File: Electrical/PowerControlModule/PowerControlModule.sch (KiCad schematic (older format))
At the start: 1 part, among them Q1 IPP120P04P4L03AKSA1

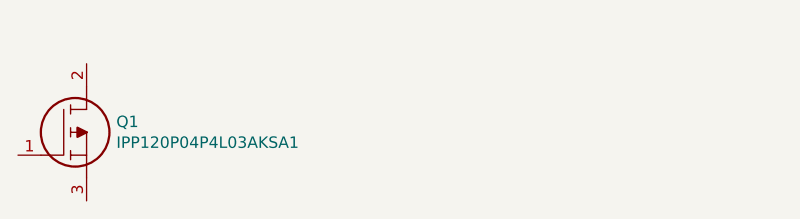
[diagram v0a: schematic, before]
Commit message: Testing import of power mosfet
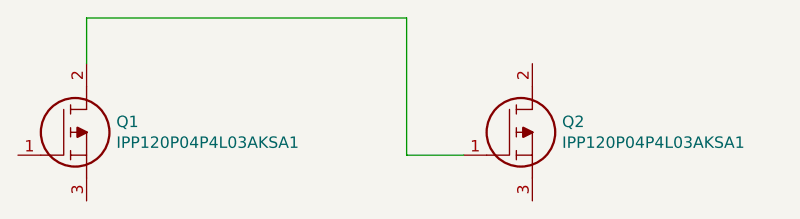
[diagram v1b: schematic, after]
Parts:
- added Q2: IPP120P04P4L03AKSA1, TO254P440X1000X2110-3P, symbol LibraryLoader:IPP120P04P4L03AKSA1
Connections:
- net at Q1.2: now also Q2.1
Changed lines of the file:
@@
 	1    0    0    -1
 $EndComp
+$Comp
+L LibraryLoader:IPP120P04P4L03AKSA1 Q2
+U 1 1 5D7A9CCC
+P 7700 3350
+F 0 "Q2" H 8130 3496 50  0000 L CNN
+F 1 "IPP120P04P4L03AKSA1" H 8130 3405 50  0000 L CNN
+F 2 "TO254P440X1000X2110-3P" H 8150 3300 50  0001 L CNN
+F 3 "https://componentsearchengine.com/Datasheets/1/IPP120P04P4L03AKSA1.pdf" H 8150 3200 50  0001 L CNN
+F 4 "MOSFET P-Ch 40V 120A OptiMOS-P2 TO-220" H 8150 3100 50  0001 L CNN "Description"
+F 5 "4.4" H 8150 3000 50  0001 L CNN "Height"
+F 6 "726-IPP120P04P4L03AK" H 8150 2900 50  0001 L CNN "Mouser Part Number"
+F 7 "https://www.mouser.com/Search/Refine.aspx?Keyword=726-IPP120P04P4L03AK" H 8150 2800 50  0001 L CNN "Mouser Price/Stock"
+F 8 "Infineon" H 8150 2700 50  0001 L CNN "Manufacturer_Name"
+F 9 "IPP120P04P4L03AKSA1" H 8150 2600 50  0001 L CNN "Manufacturer_Part_Number"
+	1    7700 3350
+	1    0    0    -1
+$EndComp
+Wire Wire Line
+	7700 3350 7450 3350
+Wire Wire Line
+	7450 3350 7450 2750
+Wire Wire Line
+	7450 2750 6050 2750
+Wire Wire Line
+	6050 2750 6050 2950
 $EndSCHEMATC

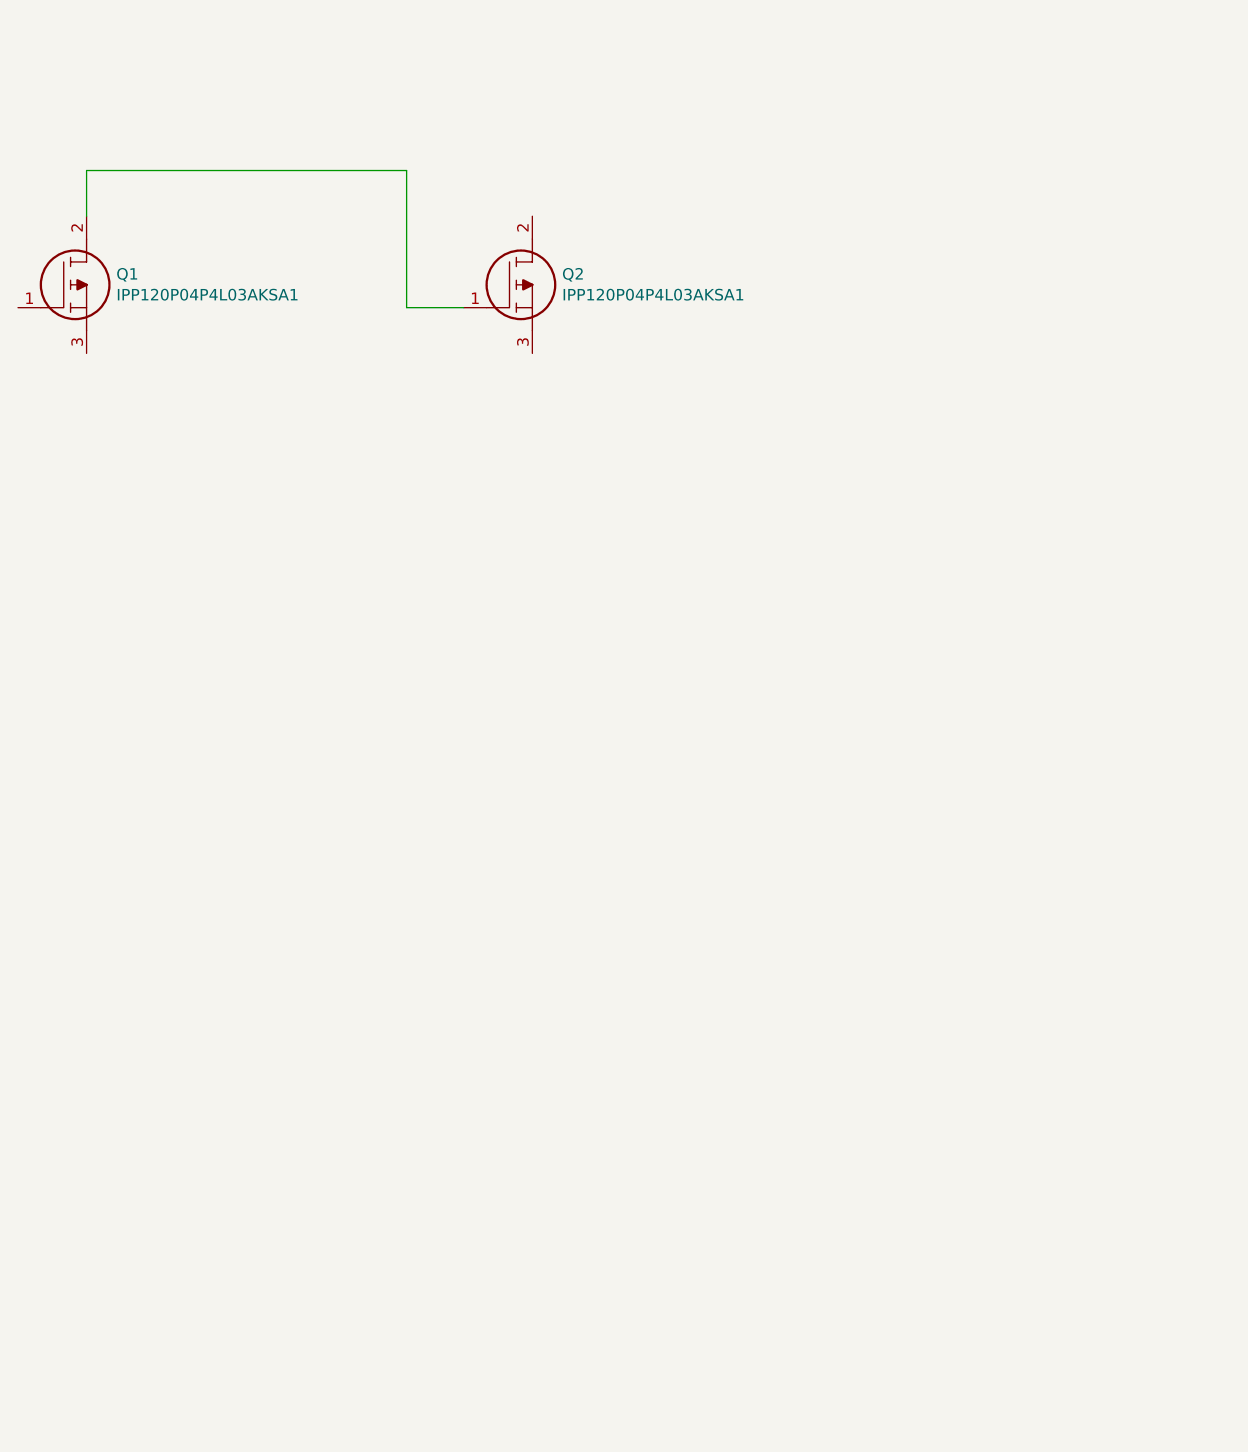
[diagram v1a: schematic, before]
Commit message: Lays out peripherals and motor control power distribution
Paginates the schematic for ease of editing
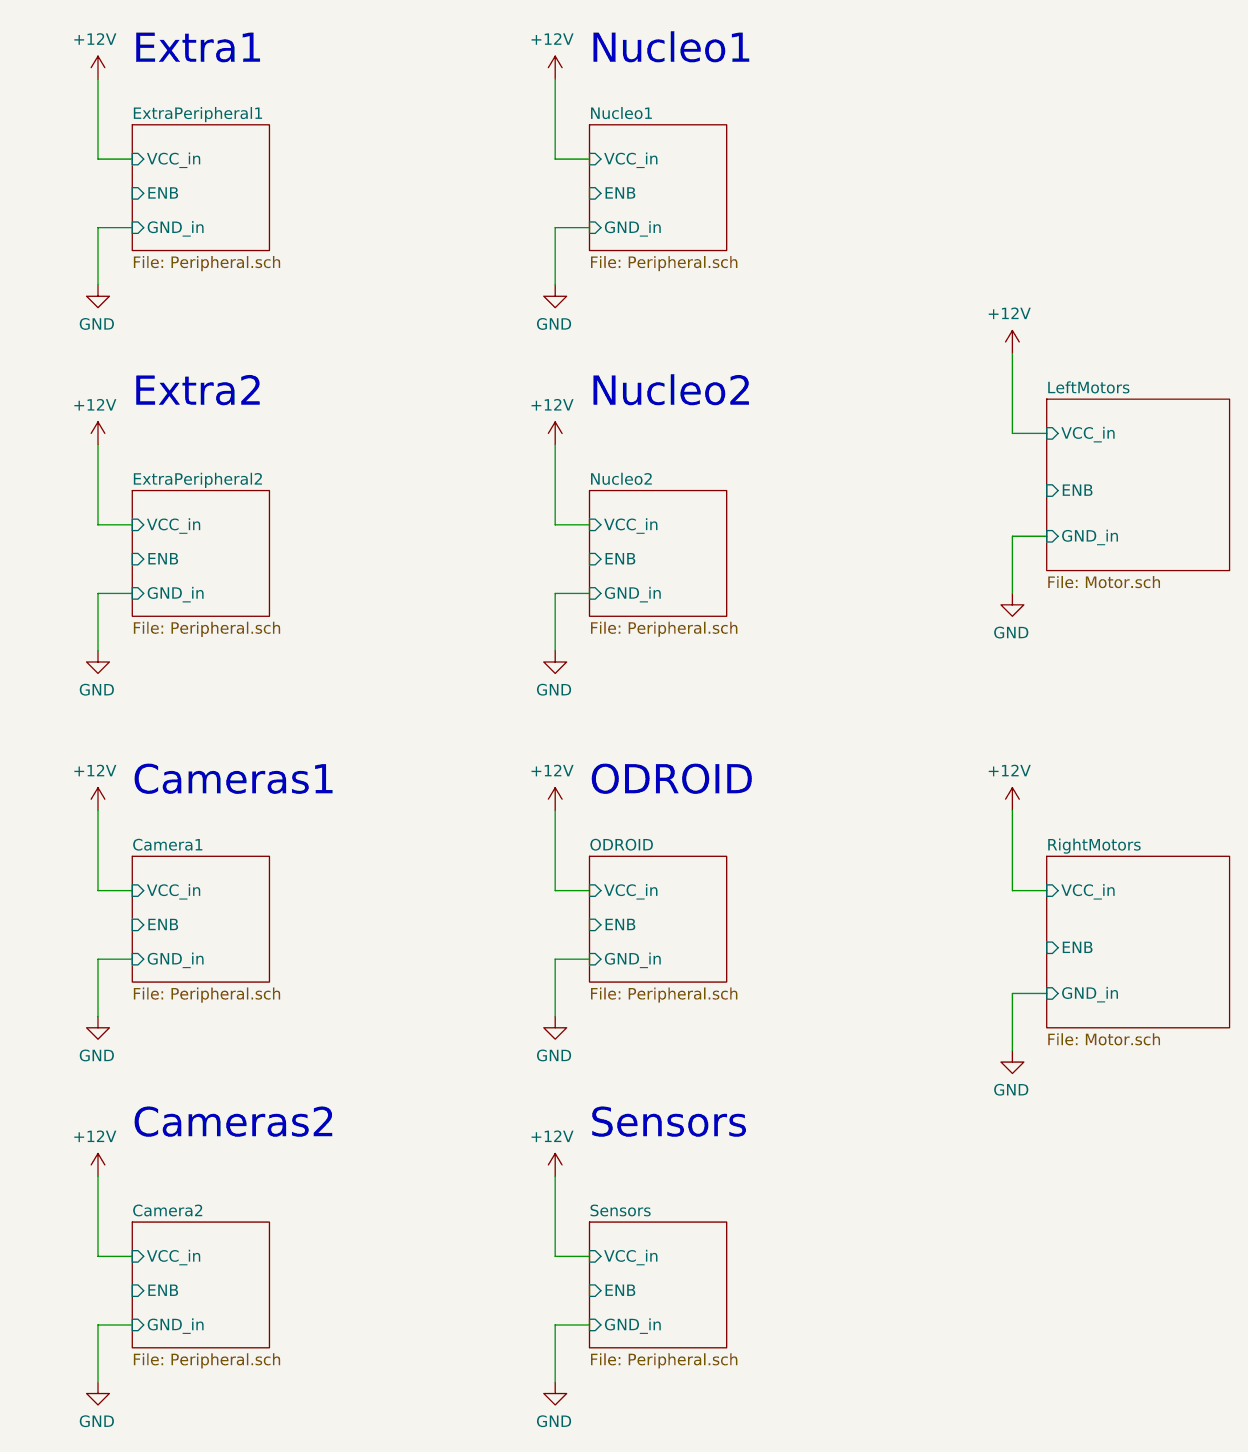
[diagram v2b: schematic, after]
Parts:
- removed Q1: IPP120P04P4L03AKSA1, LibraryLoader:TO254P440X1000X2110-3P, symbol LibraryLoader:IPP120P04P4L03AKSA1
- removed Q2: IPP120P04P4L03AKSA1, TO254P440X1000X2110-3P, symbol LibraryLoader:IPP120P04P4L03AKSA1
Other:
- note added: "Cameras1"
- note added: "Cameras2"
- note added: "Extra1"
- note added: "Extra2"
- note added: "Nucleo1"
- note added: "Nucleo2"
- note added: "ODROID"
- note added: "Sensors"

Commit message: Lays out power distribution board on PCB. Need to make 4 layer setup before routing. Also need to change motor output footprint
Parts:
- added J17: Conn_01x03, Connector_Wire:SolderWirePad_1x03_P7.62mm_Drill2.5mm, symbol Connector_Generic:Conn_01x03
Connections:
- net +12V: now also J17.1 (Pin_1)
- net GND: now also J17.3 (Pin_3)
- new net ENABLE: J17.2 (Pin_2)
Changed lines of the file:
@@
 	-1   0    0    -1
 $EndComp
+$Comp
+L power:GND #PWR022
+U 1 1 5D8A4822
+P 3200 5050
+F 0 "#PWR022" H 3200 4800 50  0001 C CNN
+F 1 "GND" H 3205 4877 50  0000 C CNN
+F 2 "" H 3200 5050 50  0001 C CNN
+F 3 "" H 3200 5050 50  0001 C CNN
+	1    3200 5050
+	-1   0    0    -1
+$EndComp
+$Comp
+L power:+12V #PWR021
+U 1 1 5D8A4828
+P 3200 4150
+F 0 "#PWR021" H 3200 4000 50  0001 C CNN
+F 1 "+12V" H 3215 4323 50  0000 C CNN
+F 2 "" H 3200 4150 50  0001 C CNN
+F 3 "" H 3200 4150 50  0001 C CNN
+	1    3200 4150
+	-1   0    0    -1
+$EndComp
+Wire Wire Line
+	3200 4550 3350 4550
+Wire Wire Line
+	3200 4150 3200 4550
+Wire Wire Line
+	3200 4750 3350 4750
+Wire Wire Line
+	3200 4750 3200 5050
+$Comp
+L Connector_Generic:Conn_01x03 J17
+U 1 1 5D8A562C
+P 3550 4650
+F 0 "J17" H 3630 4692 50  0000 L CNN
+F 1 "Conn_01x03" H 3630 4601 50  0000 L CNN
+F 2 "Connector_Wire:SolderWirePad_1x03_P7.62mm_Drill2.5mm" H 3550 4650 50  0001 C CNN
+F 3 "~" H 3550 4650 50  0001 C CNN
+	1    3550 4650
+	1    0    0    -1
+$EndComp
+Text Label 2850 4650 0    50   ~ 0
+ENABLE
+Wire Wire Line
+	3350 4650 2850 4650
+Text Label 5700 4450 0    50   ~ 0
+ENABLE
+Wire Wire Line
+	5700 4450 6250 4450
+Text Label 5700 2850 0    50   ~ 0
+ENABLE
+Wire Wire Line
+	5700 2850 6250 2850
+Text Label 5700 6050 0    50   ~ 0
+ENABLE
+Wire Wire Line
+	5700 6050 6250 6050
+Text Label 5700 7650 0    50   ~ 0
+ENABLE
+Wire Wire Line
+	5700 7650 6250 7650
+Text Label 7700 7650 0    50   ~ 0
+ENABLE
+Wire Wire Line
+	7700 7650 8250 7650
+Text Label 7700 6050 0    50   ~ 0
+ENABLE
+Wire Wire Line
+	7700 6050 8250 6050
+Text Label 7700 4450 0    50   ~ 0
+ENABLE
+Wire Wire Line
+	7700 4450 8250 4450
+Text Label 7700 2850 0    50   ~ 0
+ENABLE
+Wire Wire Line
+	7700 2850 8250 2850
+Text Label 9700 4150 0    50   ~ 0
+ENABLE
+Wire Wire Line
+	9700 4150 10250 4150
+Text Label 9700 6150 0    50   ~ 0
+ENABLE
+Wire Wire Line
+	9700 6150 10250 6150
 $EndSCHEMATC

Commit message: Power control module grounding and power plane fixes
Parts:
- renumbered J17 to PowerConnection1
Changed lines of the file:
@@
 	3200 4750 3200 5050
 $Comp
-L Connector_Generic:Conn_01x03 J17
+L Connector_Generic:Conn_01x03 PowerConnection1
 U 1 1 5D8A562C
 P 3550 4650
-F 0 "J17" H 3630 4692 50  0000 L CNN
+F 0 "PowerConnection1" H 3630 4692 50  0000 L CNN
 F 1 "Conn_01x03" H 3630 4601 50  0000 L CNN
 F 2 "Connector_Wire:SolderWirePad_1x03_P7.62mm_Drill2.5mm" H 3550 4650 50  0001 C CNN

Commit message: Splits project into multiple modules, peripherals, motors, and safety
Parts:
- added H1, H2, H3, H4: MountingHole, MountingHole:MountingHole_3.2mm_M3, symbol Mechanical:MountingHole
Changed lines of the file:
@@
 Wire Wire Line
 	9700 6150 10250 6150
+$Comp
+L Mechanical:MountingHole H1
+U 1 1 5D94753E
+P 12700 850
+F 0 "H1" H 12800 896 50  0000 L CNN
+F 1 "MountingHole" H 12800 805 50  0000 L CNN
+F 2 "MountingHole:MountingHole_3.2mm_M3" H 12700 850 50  0001 C CNN
+F 3 "~" H 12700 850 50  0001 C CNN
+	1    12700 850
+	1    0    0    -1
+$EndComp
+$Comp
+L Mechanical:MountingHole H2
+U 1 1 5D9499A3
+P 13600 850
+F 0 "H2" H 13700 896 50  0000 L CNN
+F 1 "MountingHole" H 13700 805 50  0000 L CNN
+F 2 "MountingHole:MountingHole_3.2mm_M3" H 13600 850 50  0001 C CNN
+F 3 "~" H 13600 850 50  0001 C CNN
+	1    13600 850
+	1    0    0    -1
+$EndComp
+$Comp
+L Mechanical:MountingHole H3
+U 1 1 5D94A22A
+P 14500 850
+F 0 "H3" H 14600 896 50  0000 L CNN
+F 1 "MountingHole" H 14600 805 50  0000 L CNN
+F 2 "MountingHole:MountingHole_3.2mm_M3" H 14500 850 50  0001 C CNN
+F 3 "~" H 14500 850 50  0001 C CNN
+	1    14500 850
+	1    0    0    -1
+$EndComp
+$Comp
+L Mechanical:MountingHole H4
+U 1 1 5D94ABCC
+P 15350 850
+F 0 "H4" H 15450 896 50  0000 L CNN
+F 1 "MountingHole" H 15450 805 50  0000 L CNN
+F 2 "MountingHole:MountingHole_3.2mm_M3" H 15350 850 50  0001 C CNN
+F 3 "~" H 15350 850 50  0001 C CNN
+	1    15350 850
+	1    0    0    -1
+$EndComp
 $EndSCHEMATC
